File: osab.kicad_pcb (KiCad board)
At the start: 2 copper layers, 60 x 100 mm, 152 parts, among them CON1 TF-01A, CON2 PJ-3420-A-SMT, CON3 TYPE-C-31-M-12, Q1 BC847B, SW1 PPP, SW10 RESET, SW2 VOL-, SW3 VOL+, SW4 CHAP-, SW5 CHAP+, SW6 OT/NT, SW7 BOOK-, SW8 BOOK+, SW9 BUTTON_LOCK, U1 VS1000, U2 ME6211C33M5G-N, U3 25LC640A, U4 TP4055, U5 MF5853CS, U6 TCS7191, Y1 12MHz

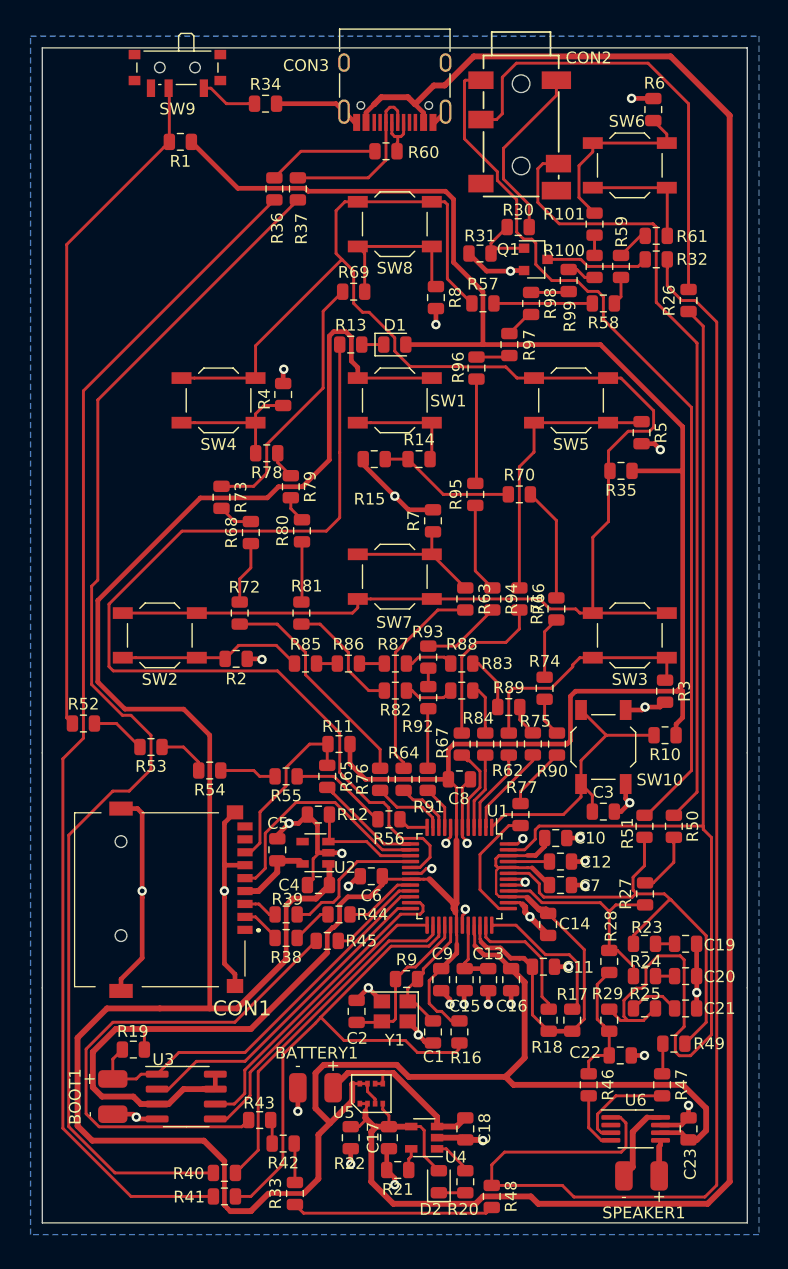
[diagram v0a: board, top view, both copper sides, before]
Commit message: single-sided: Added filled zone for front copper connected to no net
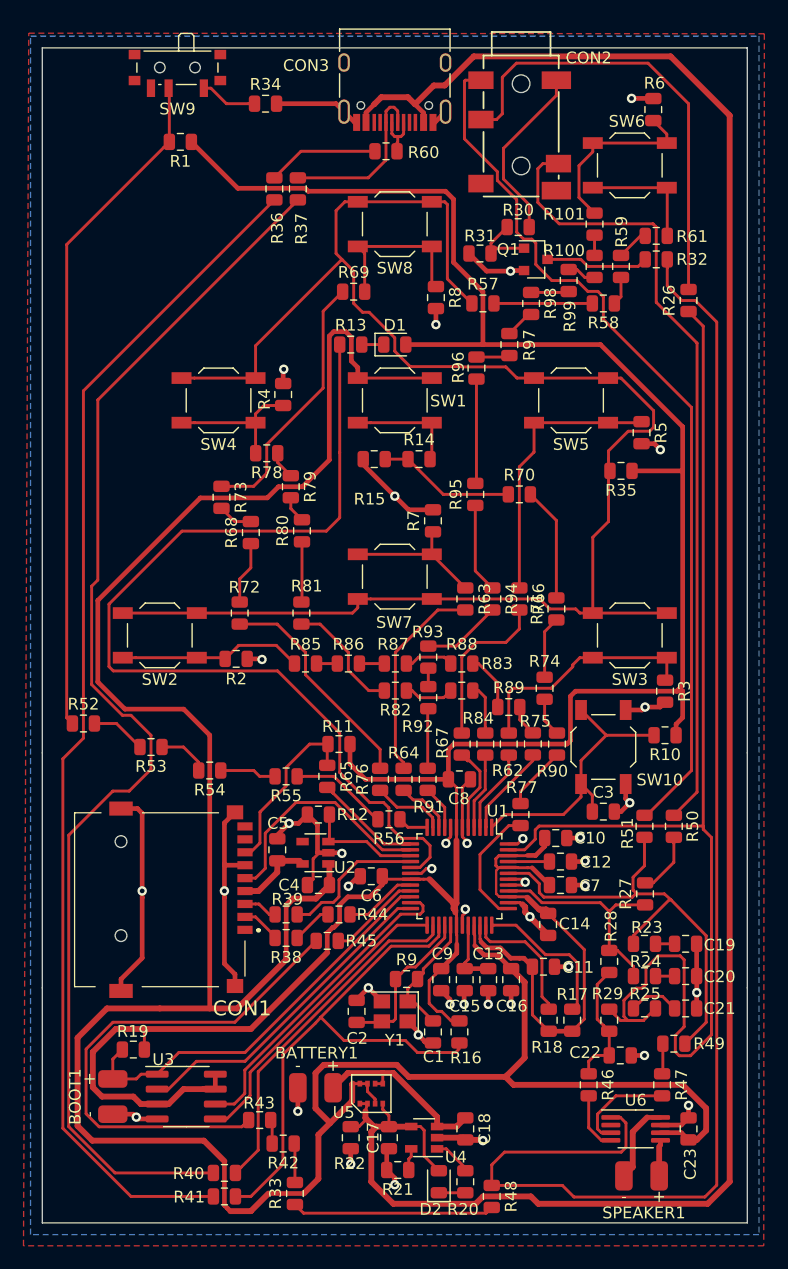
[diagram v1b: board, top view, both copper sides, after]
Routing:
- added copper zone on F.Cu, net (none)
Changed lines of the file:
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@@
     (visible_elements FFFFFF7F)
     (pcbplotparams
-      (layerselection 0x010fc_ffffffff)
+      (layerselection 0x00000_ffffffff)
       (usegerberextensions false)
       (usegerberattributes false)
       (usegerberadvancedattributes false)
       (creategerberjobfile false)
-      (excludeedgelayer true)
+      (excludeedgelayer false)
       (linewidth 0.100000)
       (plotframeref false)
@@
       (padsonsilk false)
       (subtractmaskfromsilk false)
-      (outputformat 1)
+      (outputformat 4)
       (mirror false)
       (drillshape 1)
@@
       )
     )
+  )
+  (zone (net 0) (net_name "") (layer F.Cu) (hatch edge 0.508)
+    (connect_pads (clearance 0.508))
+    (min_thickness 0.254)
+    (fill yes (arc_segments 32) (thermal_gap 0.508) (thermal_bridge_width 0.508))
+    (polygon
+      (pts
+        (xy 176.45 45.8) (xy 176.4 148.95) (xy 113.4 148.95) (xy 113.85 45.75)
+      )
+    )

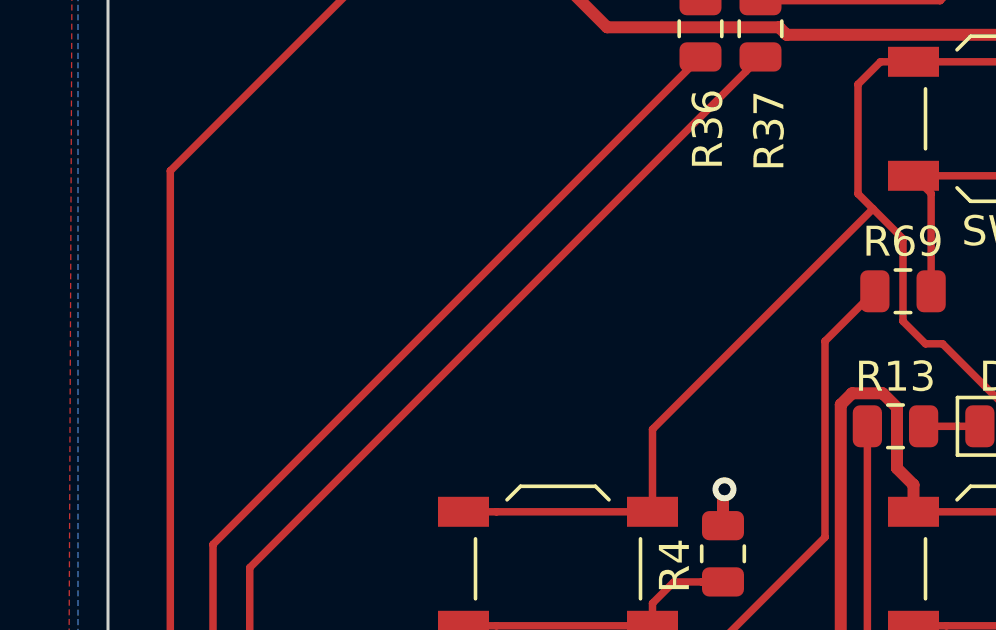
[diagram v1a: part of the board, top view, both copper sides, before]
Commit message: single-sided: Added OSAB labelling on front silkscreen
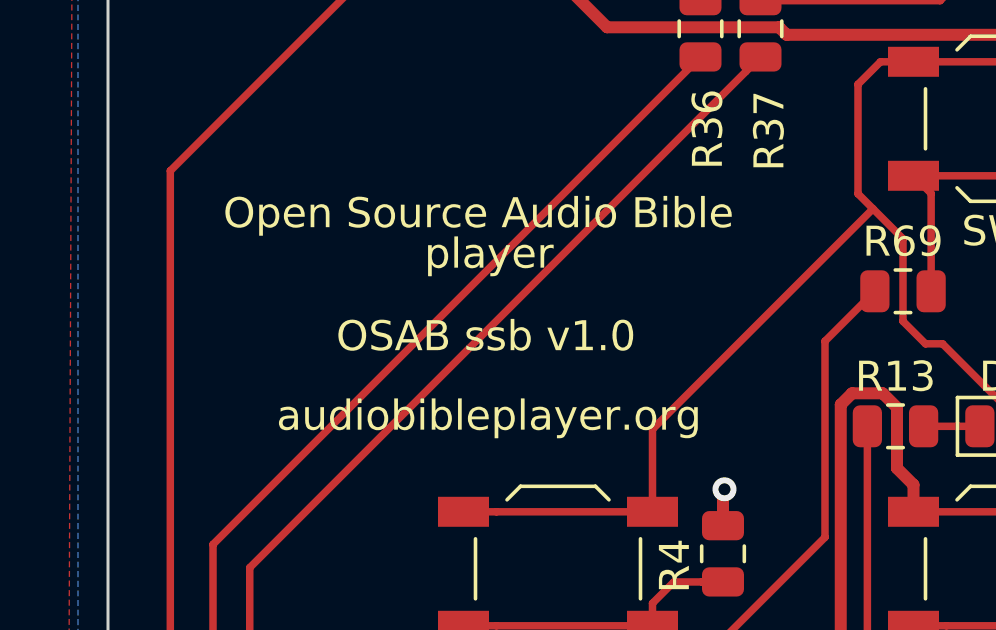
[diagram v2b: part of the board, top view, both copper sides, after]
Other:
- board text added: "OSAB ssb v1.0"
- board text added: "Open Source Audio Bible"
- board text added: "audiobibleplayer.org"
- board text added: "player"
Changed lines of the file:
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@@
   (general
     (thickness 1.6)
-    (drawings 8)
+    (drawings 12)
     (tracks 1105)
     (zones 0)
@@
     )
   )
+  (gr_text audiobibleplayer.org (at 127.7 71.9) (layer F.SilkS)
+    (effects (font (size 1 1) (thickness 0.15)))
+  )
+  (gr_text player (at 127.7 66.5) (layer F.SilkS)
+    (effects (font (size 1 1) (thickness 0.15)))
+  )
+  (gr_text "Open Source Audio Bible" (at 127.35 65.15) (layer F.SilkS)
+    (effects (font (size 1 1) (thickness 0.15)))
+  )
+  (gr_text "OSAB ssb v1.0" (at 127.6 69.25) (layer F.SilkS)
+    (effects (font (size 1 1) (thickness 0.15)))
+  )
   (gr_line (start 175 147) (end 175 127) (layer Edge.Cuts) (width 0.1))

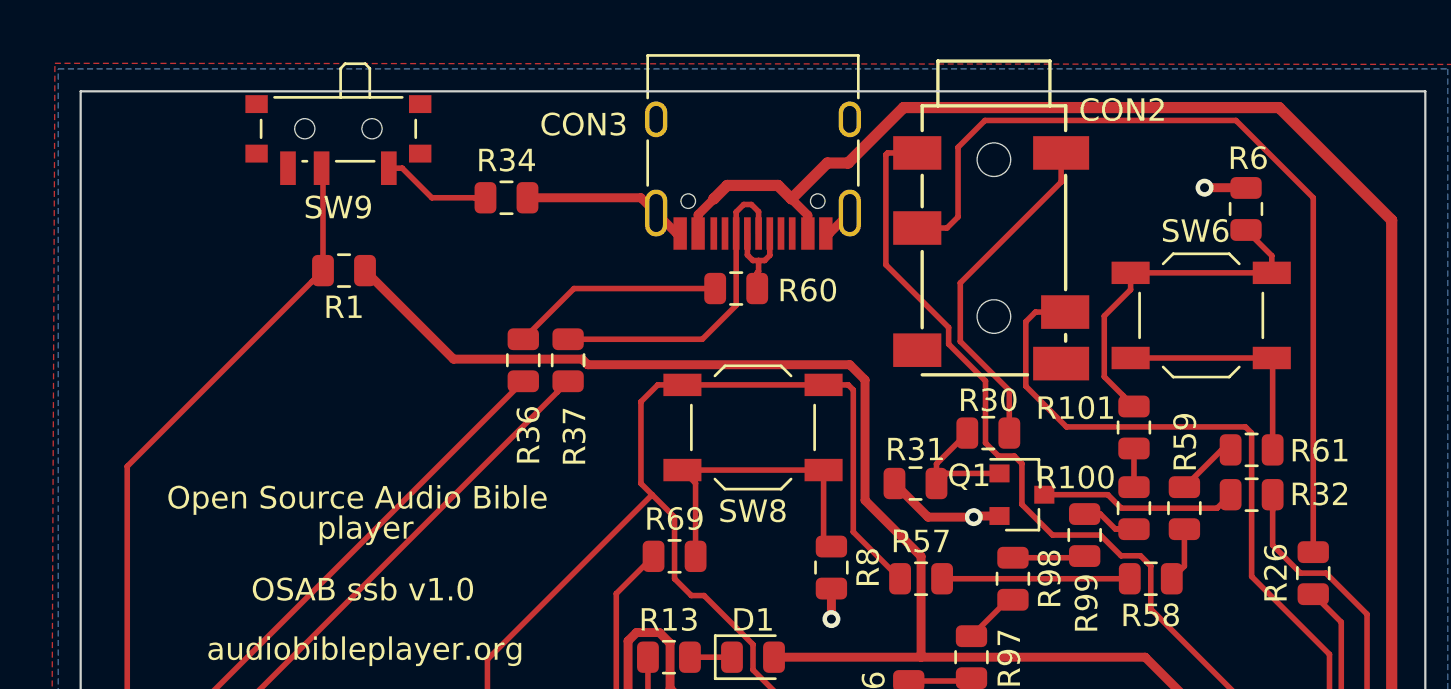
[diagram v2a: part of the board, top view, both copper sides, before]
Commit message: single-sided: Updated PJ-3420 on ssb
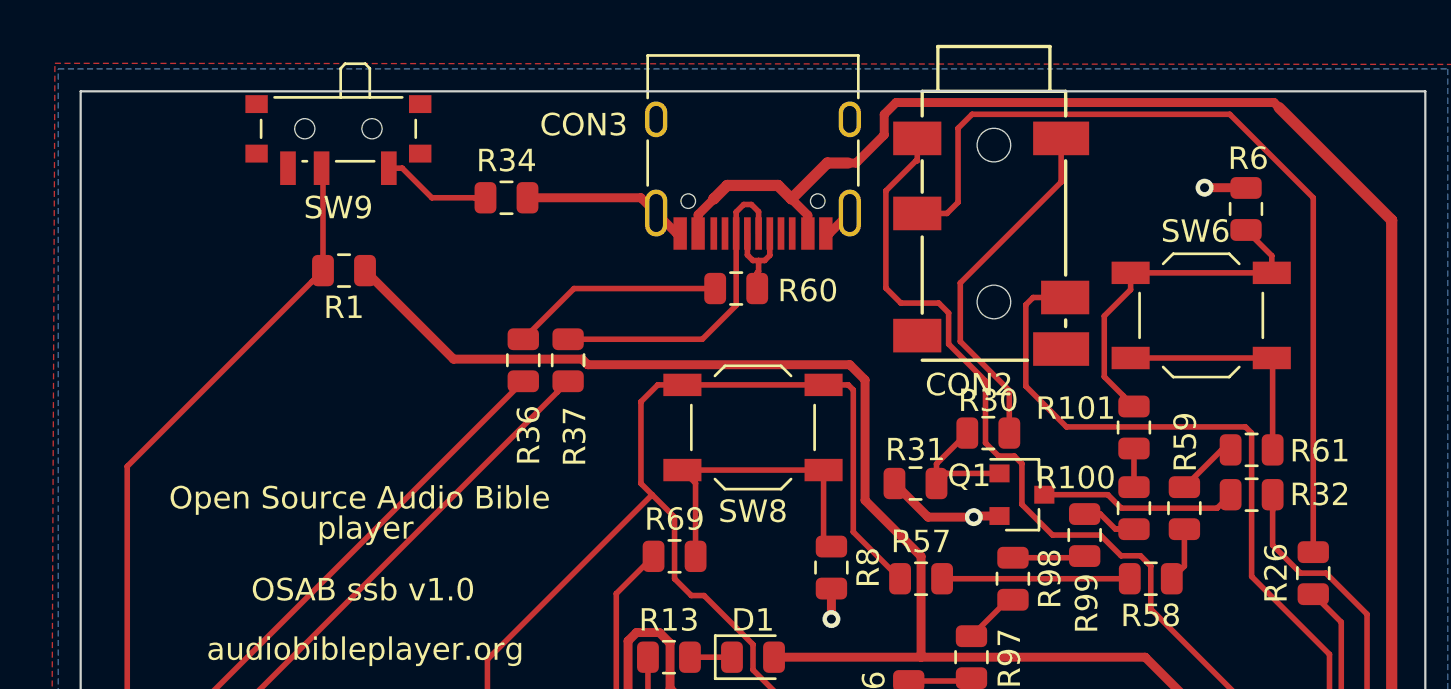
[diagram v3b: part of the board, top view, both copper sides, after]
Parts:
- moved CON2 0.65 mm to (155.8, 56.4)
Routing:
- net Net-(CON2-Pad1): track 75.9 -> 76.8 mm
- net Net-(C17-Pad1): track 181.5 -> 182.3 mm
- net Net-(CON2-Pad4): track 68.1 -> 68.8 mm
- net Net-(CON2-Pad2): track 15.3 -> 15.9 mm

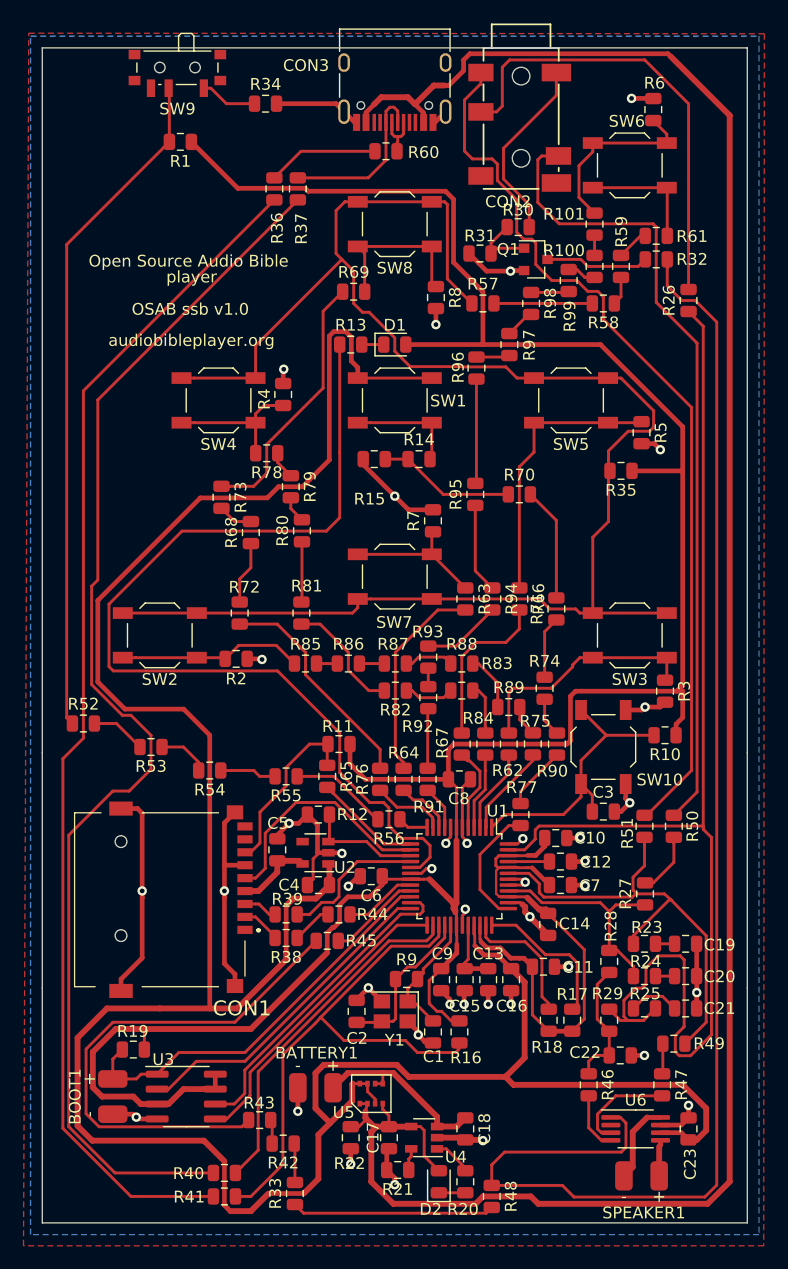
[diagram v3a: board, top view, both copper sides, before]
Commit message: single-sided: Moved earphone and USB sockets back a bit
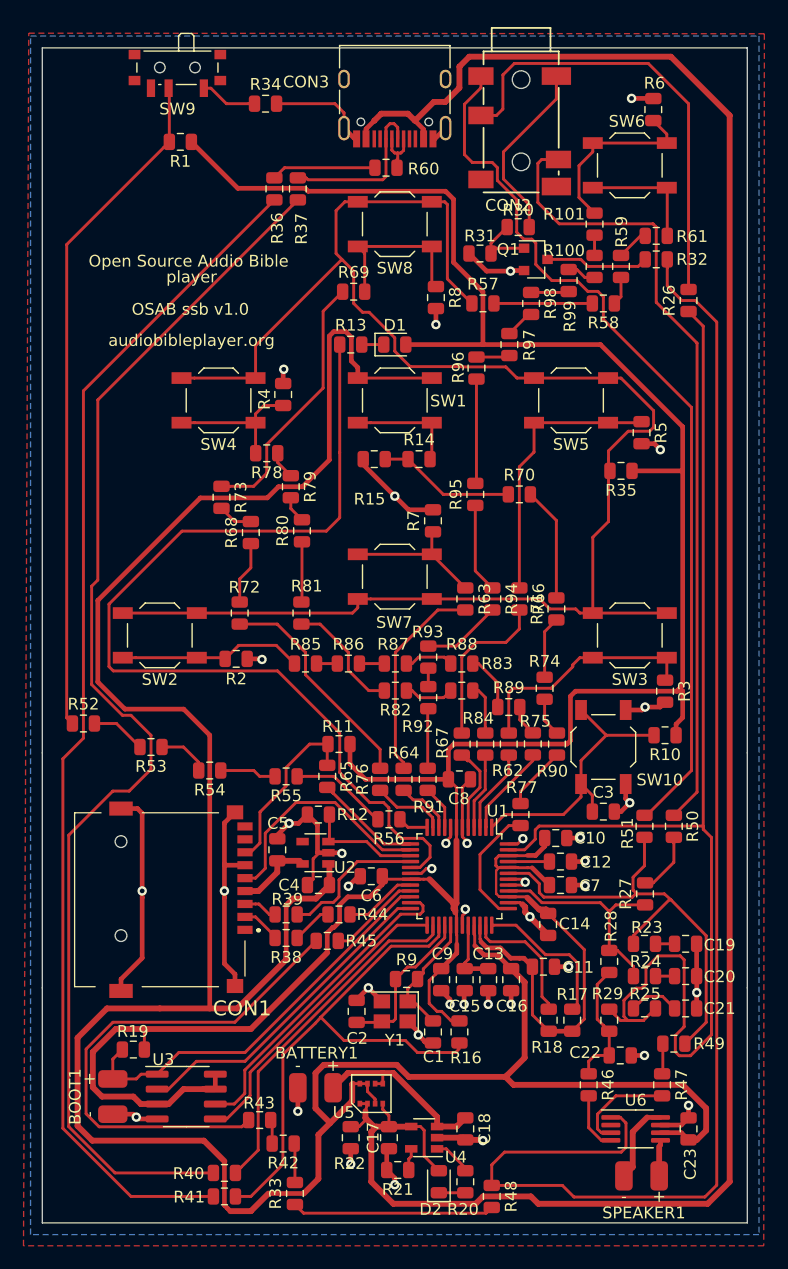
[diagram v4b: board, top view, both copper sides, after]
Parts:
- moved CON3 1.40 mm to (145.0, 50.7)
- moved R60 1.40 mm to (144.2, 57.2)
- moved CON2 0.30 mm to (155.8, 56.7)
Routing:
- net GND: track 147.6 -> 149.0 mm
- net Net-(C17-Pad1): track 182.3 -> 183.2 mm
- net Net-(R36-Pad1): track 9.50 -> 8.92 mm

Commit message: single-sided: Nudged USB socket out by 0.2 mm
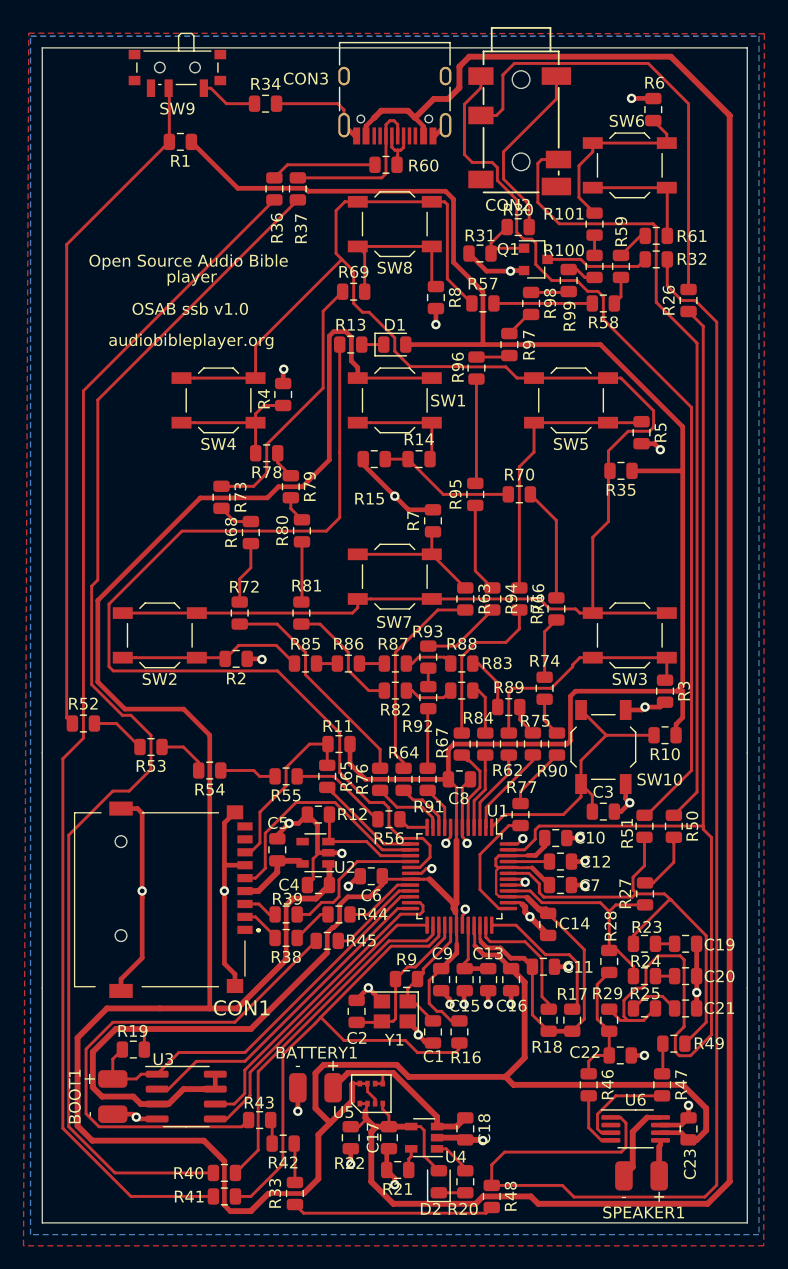
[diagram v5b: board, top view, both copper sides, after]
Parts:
- moved CON3 0.25 mm to (145.0, 50.5)
- moved R60 0.25 mm to (144.2, 57.0)
